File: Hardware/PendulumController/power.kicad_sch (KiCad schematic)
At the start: 8 parts, among them J301 19V Input, U301 NCV1117ST50T3G

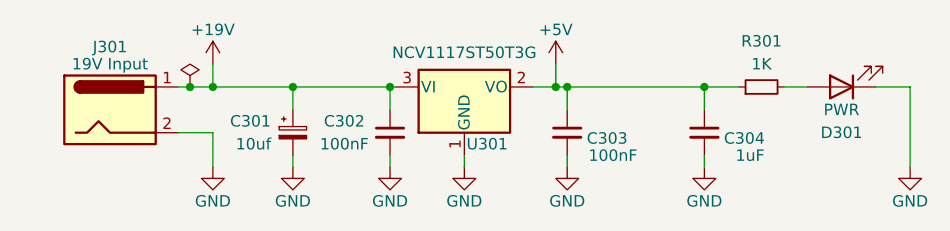
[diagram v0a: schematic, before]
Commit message: Clean up board design with embedded power supply
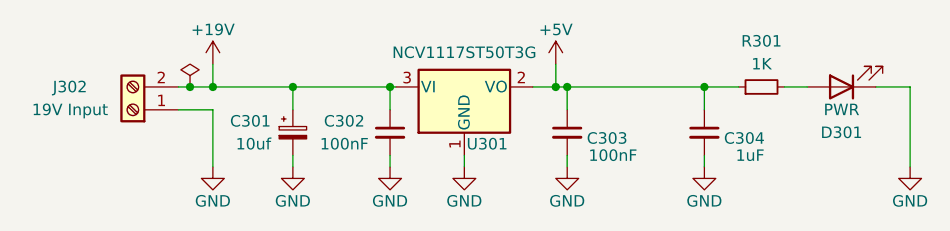
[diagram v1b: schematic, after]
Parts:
- removed J301: 19V Input, Connector_BarrelJack:BarrelJack_GCT_DCJ200-10-A_Horizontal, symbol Connector:Barrel_Jack
- added J302: 19V Input, TerminalBlock_Phoenix:TerminalBlock_Phoenix_MKDS-3-2-5.08_1x02_P5.08mm_Horizontal, symbol Connector:Screw_Terminal_01x02
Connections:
- net +19V: now also J302.2 (Pin_2)
- net GND: now also J302.1 (Pin_1)
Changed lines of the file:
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@@
     (stroke (width 0) (type default) (color 0 0 0 0))
   )
-  (wire (pts (xy 113.03 93.345) (xy 116.84 93.345))
+  (wire (pts (xy 113.03 90.805) (xy 116.84 90.805))
     (stroke (width 0) (type default) (color 0 0 0 0))
   )
-  (wire (pts (xy 116.84 97.155) (xy 116.84 93.345))
+  (wire (pts (xy 116.84 97.155) (xy 116.84 90.805))
     (stroke (width 0) (type default) (color 0 0 0 0))
   )
@@
     (stroke (width 0) (type default) (color 0 0 0 0))
   )
-  (symbol (lib_id "Connector:Barrel_Jack") (at 105.41 90.805 0) (unit 1)
+  (symbol (lib_id "Connector:Screw_Terminal_01x02") (at 107.95 90.805 180) (unit 1)
     (in_bom yes) (on_board yes)
-    (property "Reference" "J301" (id 0) (at 105.41 83.82 0))
-    (property "Value" "19V Input" (id 1) (at 105.41 85.725 0))
-    (property "Footprint" "Connector_BarrelJack:BarrelJack_GCT_DCJ200-10-A_Horizontal" (id 2) (at 106.68 91.821 0)
+    (property "Reference" "J302" (id 0) (at 100.965 88.265 0))
+    (property "Value" "19V Input" (id 1) (at 100.965 90.805 0))
+    (property "Footprint" "TerminalBlock_Phoenix:TerminalBlock_Phoenix_MKDS-3-2-5.08_1x02_P5.08mm_Horizontal" (id 2) (at 107.95 90.805 0)
       (effects (font (size 1.27 1.27)) hide)
     )
-    (property "Datasheet" "~" (id 3) (at 106.68 91.821 0)
+    (property "Datasheet" "~" (id 3) (at 107.95 90.805 0)
       (effects (font (size 1.27 1.27)) hide)
     )
